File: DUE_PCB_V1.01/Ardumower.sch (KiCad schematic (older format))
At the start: 61 parts, among them J1 I2C_1, J10 P_Left, J11 P_Right, J12 Sonar_R, J13 Sonar_C, J14 Sonar_L, J15 Bumper Left, J16 Button, J17 US1, J18 US2, J19 US3, J2 I2C_2, J20 5V IN, J21 Remote, J22 PCB_2, J23 5V Power, J24 3.3V IN, J25 3.3V Power, J26 TX0/RX0, J3 I2C_3, J31 Bumper Right, J32 TX1/RX1, J33 TX2/RX2, J34 GPS_TX/GPS_RX, J4 DS3231 RTC, J5 9V IN, J6 Drop_Left, J7 Drop_Right, J8 Tilt, J9 Rain

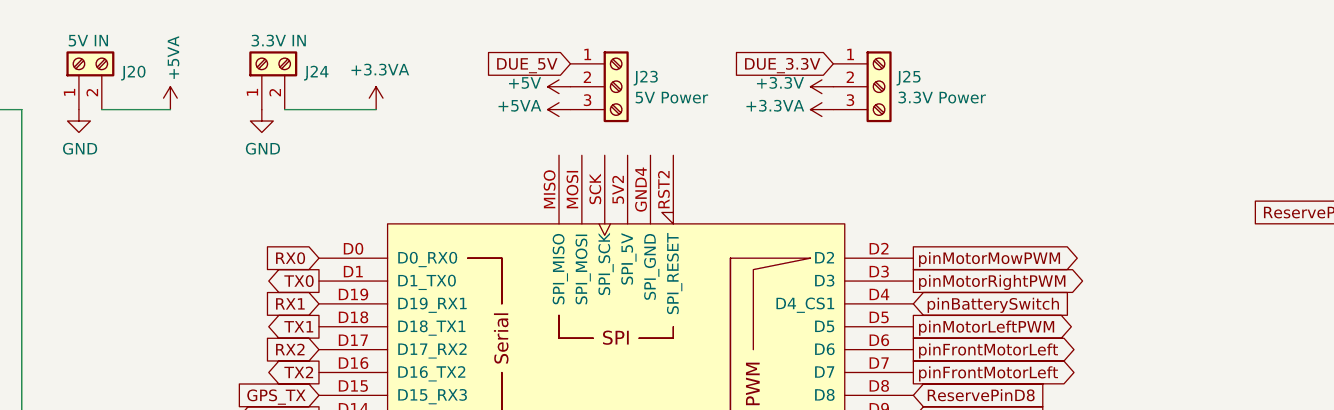
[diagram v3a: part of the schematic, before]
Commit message: Change Jumper for Power Source
Change Screw Terminal for 5V/3.3V to jumper.
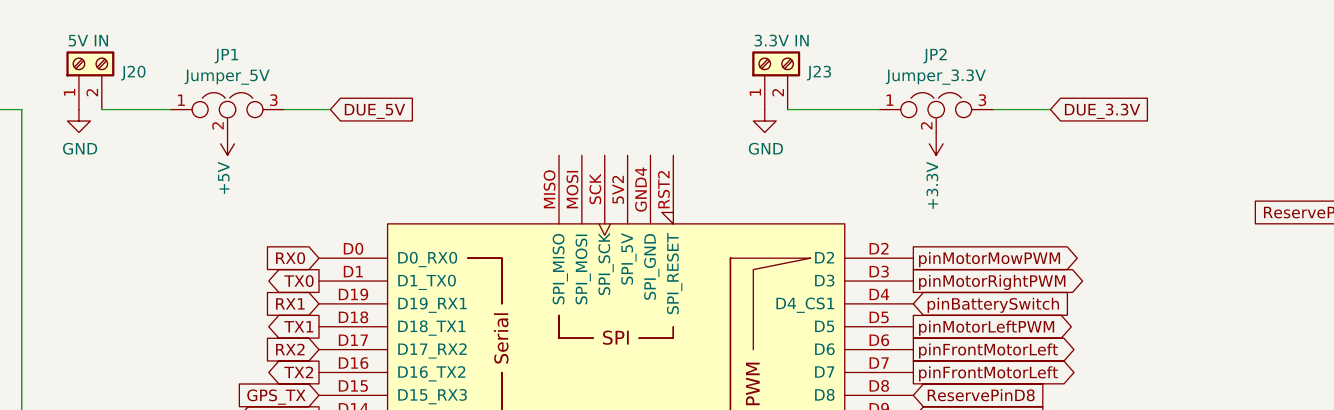
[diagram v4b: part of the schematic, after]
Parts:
- removed J23: 5V Power, Connector_PinHeader_2.54mm:PinHeader_1x03_P2.54mm_Vertical, symbol Connector:Screw_Terminal_01x03
- removed J24: 3.3V IN, TerminalBlock:TerminalBlock_bornier-2_P5.08mm, symbol Connector:Screw_Terminal_01x02
- removed J25: 3.3V Power, Connector_PinHeader_2.54mm:PinHeader_1x03_P2.54mm_Vertical, symbol Connector:Screw_Terminal_01x03
- added J23: 3.3V IN, TerminalBlock:TerminalBlock_bornier-2_P5.08mm, symbol Connector:Screw_Terminal_01x02
- added JP1: Jumper_5V, Connector_PinHeader_2.54mm:PinHeader_1x03_P2.54mm_Vertical, symbol Device:Jumper_NC_Dual
- added JP2: Jumper_3.3V, Connector_PinHeader_2.54mm:PinHeader_1x03_P2.54mm_Vertical, symbol Device:Jumper_NC_Dual
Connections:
- net +3V3: now also JP2.2
- net +5V: now also JP1.2
- net +5VA: no longer J20.2 (Pin_2)
- net DUE_3.3V: now also JP2.3
- net DUE_5V: now also JP1.3
- net GND: now also J23.1 (Pin_1)
- new net: J20.2 (Pin_2), JP1.1
- new net: J23.2 (Pin_2), JP2.1
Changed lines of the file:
@@
 	3550 5800 4850 5800
-$Comp
-L Connector:Screw_Terminal_01x02 J24
-U 1 1 6093FCF7
-P 4600 650
-F 0 "J24" V 4564 462 50  0000 R CNN
-F 1 "3.3V IN" V 4700 700 50  0000 R CNN
-F 2 "TerminalBlock:TerminalBlock_bornier-2_P5.08mm" H 4600 650 50  0001 C CNN
-F 3 "~" H 4600 650 50  0001 C CNN
-	1    4600 650
-	0    -1   -1   0
-$EndComp
-$Comp
-L power:GND #PWR042
-U 1 1 6093FD0E
-P 4600 850
-F 0 "#PWR042" H 4600 600 50  0001 C CNN
-F 1 "GND" H 4605 677 50  0000 C CNN
-F 2 "" H 4600 850 50  0001 C CNN
-F 3 "" H 4600 850 50  0001 C CNN
-	1    4600 850
-	1    0    0    -1
-$EndComp
-$Comp
-L power:GND #PWR035
-U 1 1 60943BCE
-P 3800 850
-F 0 "#PWR035" H 3800 600 50  0001 C CNN
-F 1 "GND" H 3805 677 50  0000 C CNN
-F 2 "" H 3800 850 50  0001 C CNN
-F 3 "" H 3800 850 50  0001 C CNN
-	1    3800 850
-	1    0    0    -1
-$EndComp
 $Comp
 L Connector:Screw_Terminal_01x03 J10
@@
 	1    0    0    -1
 $EndComp
-$Comp
-L power:+5VA #PWR040
-U 1 1 609619C9
-P 4200 850
-F 0 "#PWR040" H 4200 700 50  0001 C CNN
-F 1 "+5VA" V 4215 977 50  0000 L CNN
-F 2 "" H 4200 850 50  0001 C CNN
-F 3 "" H 4200 850 50  0001 C CNN
-	1    4200 850
-	1    0    0    -1
-$EndComp
 Wire Wire Line
 	2550 1000 2550 1200
@@
 Wire Wire Line
 	2550 3600 2550 3750
-$Comp
-L power:+3.3VA #PWR050
-U 1 1 609E46D2
-P 5100 850
-F 0 "#PWR050" H 5100 700 50  0001 C CNN
-F 1 "+3.3VA" H 5115 1023 50  0000 C CNN
-F 2 "" H 5100 850 50  0001 C CNN
-F 3 "" H 5100 850 50  0001 C CNN
-	1    5100 850
-	1    0    0    -1
-$EndComp
 Wire Wire Line
 	-500 7150 -150 7150
-$Comp
-L Connector:Screw_Terminal_01x02 J20
-U 1 1 60943BB7
-P 3800 650
-F 0 "J20" V 3764 462 50  0000 R CNN
-F 1 "5V IN" V 3900 700 50  0000 R CNN
-F 2 "TerminalBlock:TerminalBlock_bornier-2_P5.08mm" H 3800 650 50  0001 C CNN
-F 3 "~" H 3800 650 50  0001 C CNN
-	1    3800 650
-	0    -1   -1   0
-$EndComp
 $Comp
 L power:+3.3VA #PWR052
@@
 Wire Wire Line
 	900  850  3550 850
-Wire Wire Line
-	3900 850  4200 850
-Wire Wire Line
-	4700 850  5100 850
 $Comp
 L Device:R R12
@@
 Text GLabel 10350 3250 2    50   Input ~ 0
 DUE_5V
-$Comp
-L Connector:Screw_Terminal_01x03 J23
-U 1 1 609EC3DF
-P 6150 750
-F 0 "J23" H 6230 792 50  0000 L CNN
-F 1 "5V Power" H 6230 701 50  0000 L CNN
-F 2 "Connector_PinHeader_2.54mm:PinHeader_1x03_P2.54mm_Vertical" H 6150 750 50  0001 C CNN
-F 3 "~" H 6150 750 50  0001 C CNN
-	1    6150 750
-	1    0    0    -1
-$EndComp
-$Comp
-L power:+5VA #PWR041
-U 1 1 609EFC4F
-P 5950 850
-F 0 "#PWR041" H 5950 700 50  0001 C CNN
-F 1 "+5VA" V 5965 977 50  0000 L CNN
-F 2 "" H 5950 850 50  0001 C CNN
-F 3 "" H 5950 850 50  0001 C CNN
-	1    5950 850
-	0    -1   -1   0
-$EndComp
-Text GLabel 5950 650  0    50   Input ~ 0
-DUE_5V
-$Comp
-L Connector:Screw_Terminal_01x03 J25
-U 1 1 60A17D66
-P 7300 750
-F 0 "J25" H 7380 792 50  0000 L CNN
-F 1 "3.3V Power" H 7380 701 50  0000 L CNN
-F 2 "Connector_PinHeader_2.54mm:PinHeader_1x03_P2.54mm_Vertical" H 7300 750 50  0001 C CNN
-F 3 "~" H 7300 750 50  0001 C CNN
-	1    7300 750
-	1    0    0    -1
-$EndComp
-Text GLabel 7100 650  0    50   Input ~ 0
-DUE_3.3V
 Wire Wire Line
 	3550 850  3550 5800
@@
 $EndComp
 $Comp
-L power:+3.3VA #PWR044
-U 1 1 60A31825
-P 7100 850
-F 0 "#PWR044" H 7100 700 50  0001 C CNN
-F 1 "+3.3VA" V 7115 977 50  0000 L CNN
-F 2 "" H 7100 850 50  0001 C CNN
-F 3 "" H 7100 850 50  0001 C CNN
-	1    7100 850
-	0    -1   -1   0
-$EndComp
-$Comp
-L power:+3.3V #PWR043
-U 1 1 60A378F8
-P 7100 750
-F 0 "#PWR043" H 7100 600 50  0001 C CNN
-F 1 "+3.3V" V 7115 878 50  0000 L CNN
-F 2 "" H 7100 750 50  0001 C CNN
-F 3 "" H 7100 750 50  0001 C CNN
-	1    7100 750
-	0    -1   -1   0
-$EndComp
-$Comp
-L power:+5V #PWR039
-U 1 1 60A3E518
-P 5950 750
-F 0 "#PWR039" H 5950 600 50  0001 C CNN
-F 1 "+5V" V 5965 878 50  0000 L CNN
-F 2 "" H 5950 750 50  0001 C CNN
-F 3 "" H 5950 750 50  0001 C CNN
-	1    5950 750
-	0    -1   -1   0
-$EndComp
-$Comp
 L power:+5V #PWR024
 U 1 1 60A434DB
@@
 	0    1    1    0
 $EndComp
+$Comp
+L Device:Jumper_NC_Dual JP1
+U 1 1 60B975FC
+P 4450 850
+F 0 "JP1" H 4450 1089 50  0000 C CNN
+F 1 "Jumper_5V" H 4450 998 50  0000 C CNN
+F 2 "Connector_PinHeader_2.54mm:PinHeader_1x03_P2.54mm_Vertical" H 4450 850 50  0001 C CNN
+F 3 "~" H 4450 850 50  0001 C CNN
+	1    4450 850
+	1    0    0    -1
+$EndComp
+$Comp
+L Device:Jumper_NC_Dual JP2
+U 1 1 60B98CB4
+P 7550 850
+F 0 "JP2" H 7550 1089 50  0000 C CNN
+F 1 "Jumper_3.3V" H 7550 998 50  0000 C CNN
+F 2 "Connector_PinHeader_2.54mm:PinHeader_1x03_P2.54mm_Vertical" H 7550 850 50  0001 C CNN
+F 3 "~" H 7550 850 50  0001 C CNN
+	1    7550 850
+	1    0    0    -1
+$EndComp
+$Comp
+L power:GND #PWR035
+U 1 1 60B9BA6C
+P 3800 850
+F 0 "#PWR035" H 3800 600 50  0001 C CNN
+F 1 "GND" H 3805 677 50  0000 C CNN
+F 2 "" H 3800 850 50  0001 C CNN
+F 3 "" H 3800 850 50  0001 C CNN
+	1    3800 850
+	1    0    0    -1
+$EndComp
+$Comp
+L Connector:Screw_Terminal_01x02 J20
+U 1 1 60B9C602
+P 3800 650
+F 0 "J20" V 3764 462 50  0000 R CNN
+F 1 "5V IN" V 3900 700 50  0000 R CNN
+F 2 "TerminalBlock:TerminalBlock_bornier-2_P5.08mm" H 3800 650 50  0001 C CNN
+F 3 "~" H 3800 650 50  0001 C CNN
+	1    3800 650
+	0    -1   -1   0
+$EndComp
+Wire Wire Line
+	3900 850  4200 850
+Wire Wire Line
+	4700 850  4900 850
+$Comp
+L power:+5V #PWR039
+U 1 1 60BA71F4
+P 4450 950
+F 0 "#PWR039" H 4450 800 50  0001 C CNN
+F 1 "+5V" V 4465 1078 50  0000 L CNN
+F 2 "" H 4450 950 50  0001 C CNN
+F 3 "" H 4450 950 50  0001 C CNN
+	1    4450 950
+	-1   0    0    1
+$EndComp
+Text GLabel 4900 850  2    50   Input ~ 0
+DUE_5V
+$Comp
+L Connector:Screw_Terminal_01x02 J23
+U 1 1 60BBB17E
+P 6800 650
+F 0 "J23" V 6764 462 50  0000 R CNN
+F 1 "3.3V IN" V 6900 700 50  0000 R CNN
+F 2 "TerminalBlock:TerminalBlock_bornier-2_P5.08mm" H 6800 650 50  0001 C CNN
+F 3 "~" H 6800 650 50  0001 C CNN
+	1    6800 650
+	0    -1   -1   0
+$EndComp
+$Comp
+L power:GND #PWR040
+U 1 1 60BBBCE0
+P 6800 850
+F 0 "#PWR040" H 6800 600 50  0001 C CNN
+F 1 "GND" H 6805 677 50  0000 C CNN
+F 2 "" H 6800 850 50  0001 C CNN
+F 3 "" H 6800 850 50  0001 C CNN
+	1    6800 850
+	1    0    0    -1
+$EndComp
+Wire Wire Line
+	6900 850  7300 850
+Text GLabel 8050 850  2    50   Input ~ 0
+DUE_3.3V
+Wire Wire Line
+	7800 850  8050 850
+$Comp
+L power:+3.3V #PWR041
+U 1 1 60BC6357
+P 7550 950
+F 0 "#PWR041" H 7550 800 50  0001 C CNN
+F 1 "+3.3V" V 7565 1078 50  0000 L CNN
+F 2 "" H 7550 950 50  0001 C CNN
+F 3 "" H 7550 950 50  0001 C CNN
+	1    7550 950
+	-1   0    0    1
+$EndComp
 $EndSCHEMATC

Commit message: Change LED Power Source
Change the Power Source from the LED_5V and LED_3.3V
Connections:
- net +3.3VA is gone; now on net +3V3: R14.2
- net +5VA is gone; now on net +5V: R15.2
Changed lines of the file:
@@
 Wire Wire Line
 	-500 7150 -150 7150
-$Comp
-L power:+3.3VA #PWR052
-U 1 1 60A913E3
-P 10400 2800
-F 0 "#PWR052" H 10400 2650 50  0001 C CNN
-F 1 "+3.3VA" V 10415 2928 50  0000 L CNN
-F 2 "" H 10400 2800 50  0001 C CNN
-F 3 "" H 10400 2800 50  0001 C CNN
-	1    10400 2800
-	0    1    1    0
-$EndComp
 Wire Wire Line
 	10400 3650 10250 3650
-$Comp
-L power:+5VA #PWR053
-U 1 1 60A9B4BA
-P 10400 3650
-F 0 "#PWR053" H 10400 3500 50  0001 C CNN
-F 1 "+5VA" V 10415 3778 50  0000 L CNN
-F 2 "" H 10400 3650 50  0001 C CNN
-F 3 "" H 10400 3650 50  0001 C CNN
-	1    10400 3650
-	0    1    1    0
-$EndComp
 $Comp
 L Mechanical:MountingHole_Pad H2
@@
 	-1   0    0    1
 $EndComp
+$Comp
+L power:+3.3V #PWR?
+U 1 1 60C0713D
+P 10400 2800
+F 0 "#PWR?" H 10400 2650 50  0001 C CNN
+F 1 "+3.3V" V 10415 2928 50  0000 L CNN
+F 2 "" H 10400 2800 50  0001 C CNN
+F 3 "" H 10400 2800 50  0001 C CNN
+	1    10400 2800
+	0    1    1    0
+$EndComp
+$Comp
+L power:+5V #PWR?
+U 1 1 60C0D323
+P 10400 3650
+F 0 "#PWR?" H 10400 3500 50  0001 C CNN
+F 1 "+5V" V 10415 3778 50  0000 L CNN
+F 2 "" H 10400 3650 50  0001 C CNN
+F 3 "" H 10400 3650 50  0001 C CNN
+	1    10400 3650
+	0    1    1    0
+$EndComp
 $EndSCHEMATC

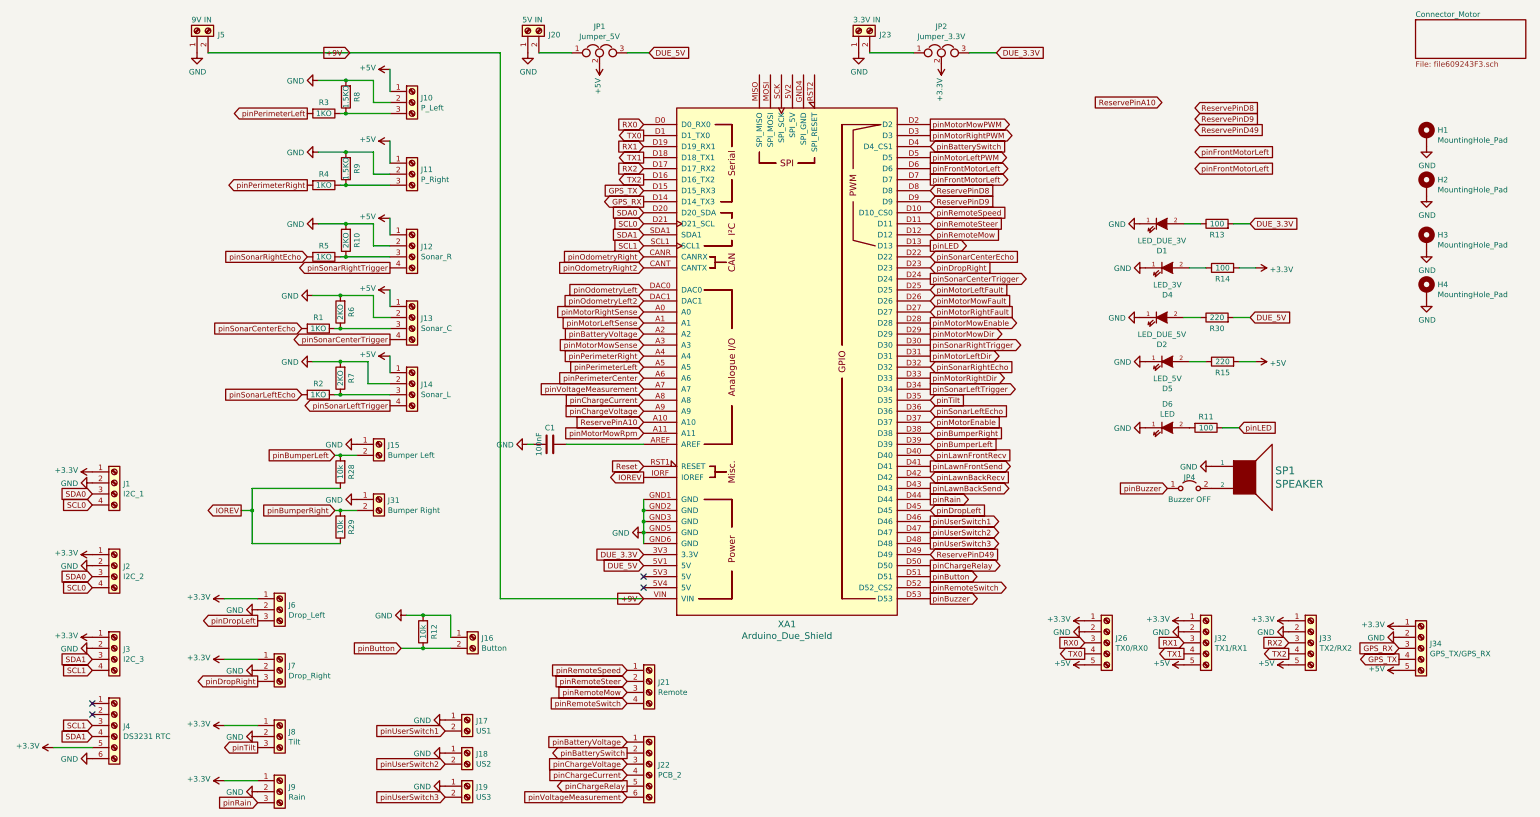
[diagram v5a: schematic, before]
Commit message: Change D6 and D7
Add Description for PIN D6 and D7 to pinFrontMotorLeft and pinFrontMotorRight
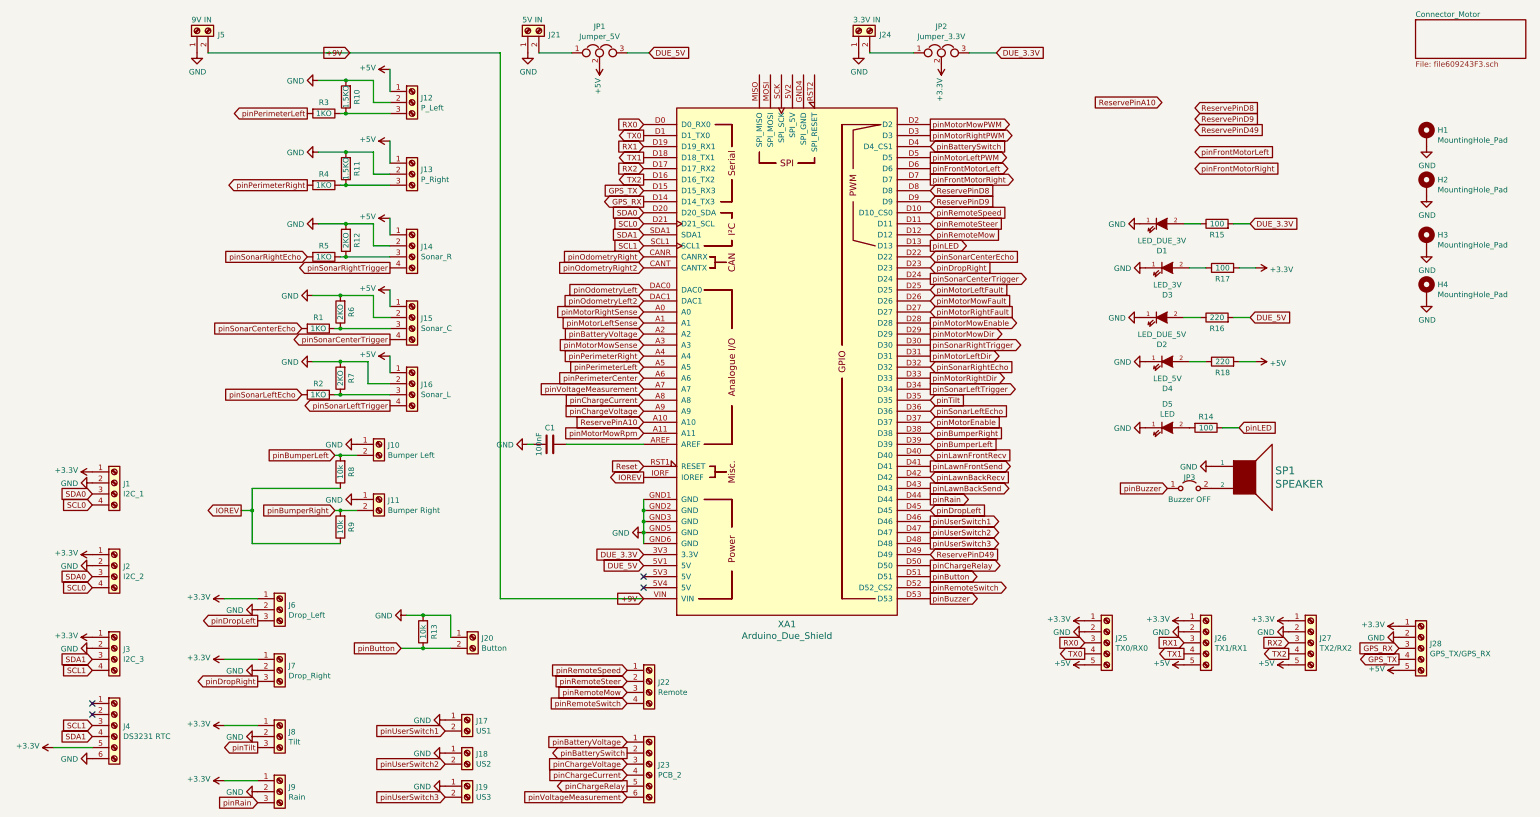
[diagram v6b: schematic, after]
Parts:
- renumbered D4 to D3, D5 to D4, D6 to D5, J15 to J10, J31 to J11, J10 to J12, J11 to J13, J12 to J14, J13 to J15, J14 to J16, J16 to J20, J20 to J21, J21 to J22, J22 to J23, J23 to J24, J26 to J25, J32 to J26, J33 to J27, J34 to J28, JP4 to JP3, R8 to R10, R9 to R11, R10 to R12, R12 to R13, R11 to R14, R13 to R15, R30 to R16, R14 to R17, R15 to R18, R28 to R8, R29 to R9
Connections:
- net pinFrontMotorLeft: no longer XA1.D7
- new net pinFrontMotorRight: XA1.D7

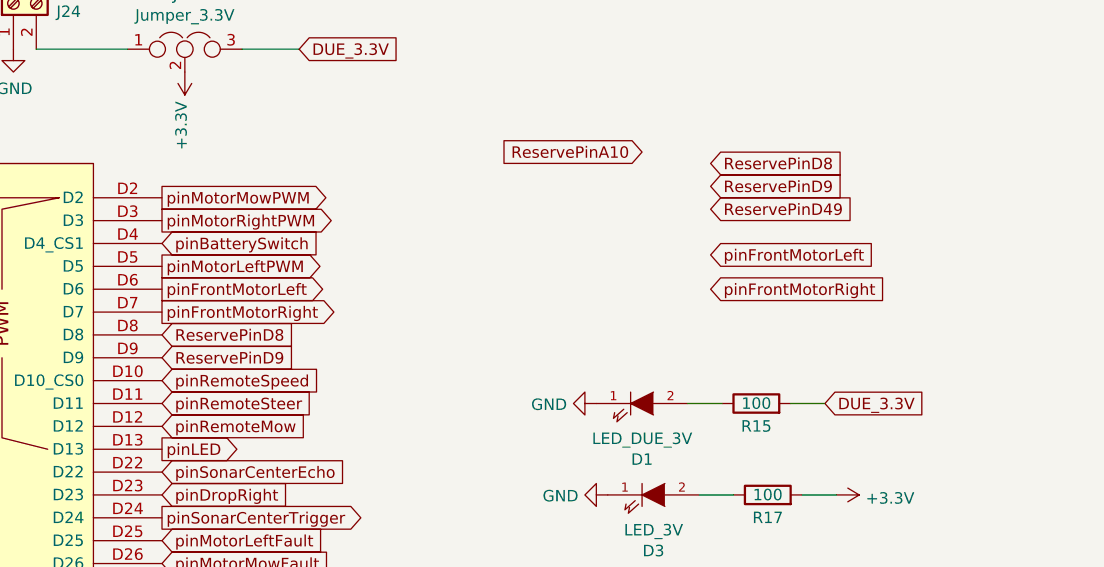
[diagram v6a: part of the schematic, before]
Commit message: Rename Pins
Rename pinFrontMotorLeft to pinMotorLeft2PWM and pinFrontMotorRight to pinMotorRight2PWM
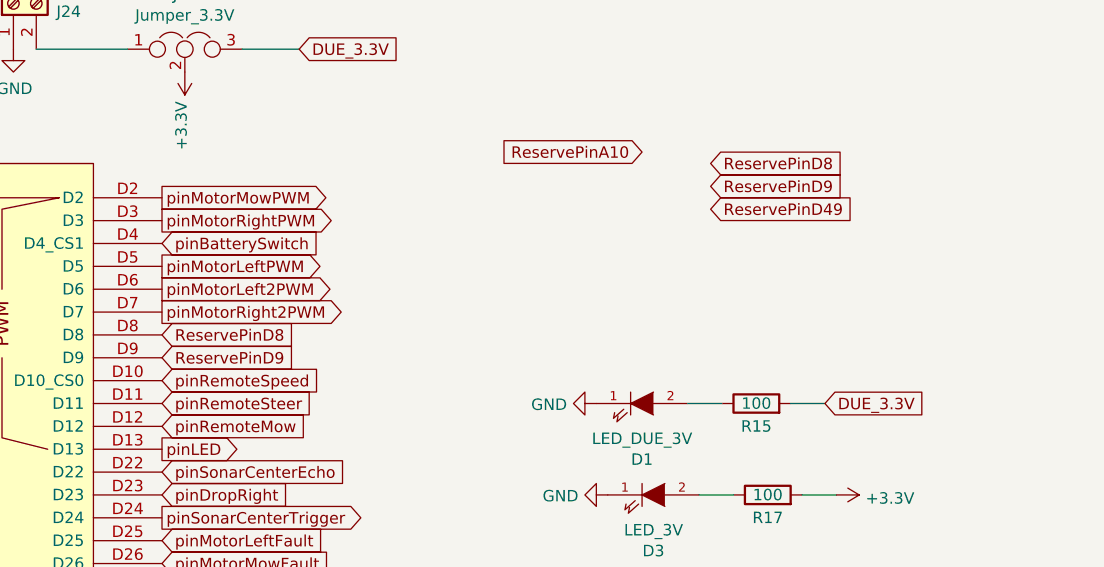
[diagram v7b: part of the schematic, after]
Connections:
- net pinFrontMotorLeft renamed pinMotorLeft2PWM
- net pinFrontMotorRight renamed pinMotorRight2PWM
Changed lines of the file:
@@
 pinPerimeterCenter
 Text GLabel 7450 1900 2    50   Output ~ 0
-pinFrontMotorLeft
+pinMotorLeft2PWM
 Text GLabel 7450 2000 2    50   Output ~ 0
-pinFrontMotorRight
+pinMotorRight2PWM
 Text GLabel 7450 2600 2    50   Output ~ 0
 pinLED
@@
 Wire Wire Line
 	10100 4250 10250 4250
-Text GLabel 9850 1750 2    50   Input ~ 0
-pinFrontMotorLeft
-Text GLabel 9850 1900 2    50   Input ~ 0
-pinFrontMotorRight
 $Comp
 L power:GND #PWR046

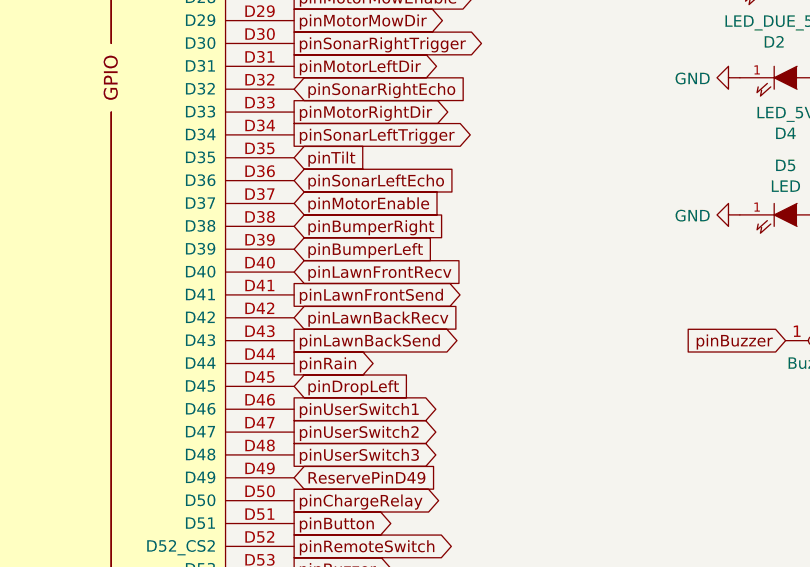
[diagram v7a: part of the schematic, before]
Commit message: Remove Lawn Sense Pins
Remove Lawn Sense Pins and add pinMotorLeft2Dir and pinMotorRight2Dir
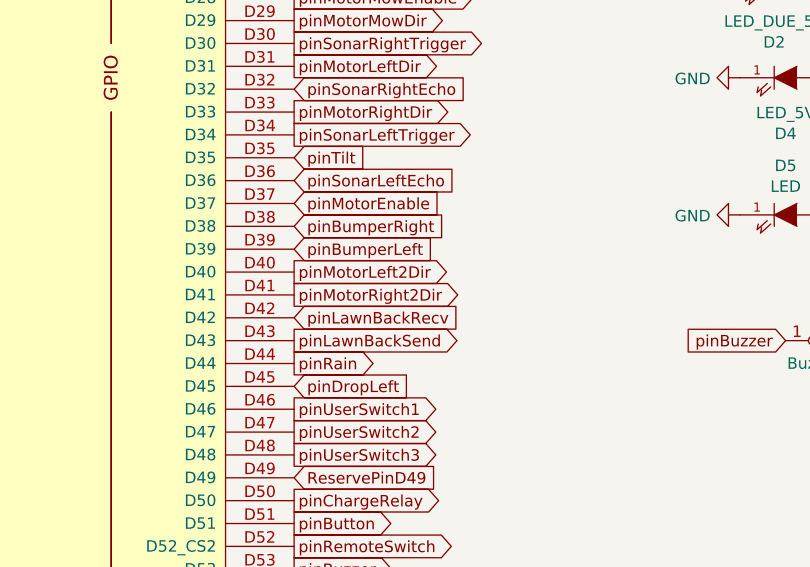
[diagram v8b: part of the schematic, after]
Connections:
- net pinLawnFrontRecv renamed pinMotorLeft2Dir
- net pinLawnFrontSend renamed pinMotorRight2Dir
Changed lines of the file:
@@
 Text GLabel 4850 3900 0    50   Input ~ 0
 pinVoltageMeasurement
-Text GLabel 7450 4500 2    50   Input ~ 0
-pinLawnFrontRecv
+Text GLabel 7450 4500 2    50   Output ~ 0
+pinMotorLeft2Dir
 Text GLabel 7450 4600 2    50   Output ~ 0
-pinLawnFrontSend
+pinMotorRight2Dir
 Text GLabel 7450 4700 2    50   Input ~ 0
 pinLawnBackRecv
